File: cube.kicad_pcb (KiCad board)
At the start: 2 copper layers, 300 parts, among them J1 serial_conn, J10 Conn_01x01, J11 Conn_01x01, J2 shifters_common_conn, J3 Conn_01x01, J4 Conn_01x01, J5 Conn_01x01, J6 Conn_01x01, J7 Conn_01x01, J8 Conn_01x01, J9 Conn_01x01, Q1 IRF9540N, Q2 IRF9540N, Q3 IRF9540N, Q4 IRF9540N, Q5 IRF9540N, Q6 IRF9540N, Q7 IRF9540N, Q8 IRF9540N, U1 SN74HC595N_0_b, U10 SN74HC595N_3_b, U11 SN74HC595N_3_g, U12 SN74HC595N_3_r, U13 SN74HC595N_4_b, U14 SN74HC595N_4_g, U15 SN74HC595N_4_r, U16 SN74HC595N_5_b, U17 SN74HC595N_5_g, U18 SN74HC595N_5_r, U19 SN74HC595N_6_b, U2 SN74HC595N_0_g, U20 SN74HC595N_6_g, U21 SN74HC595N_6_r, U22 SN74HC595N_7_b, U23 SN74HC595N_7_g, U24 SN74HC595N_7_r, U25 SN74HC595N_cols, U3 SN74HC595N_0_r, U4 SN74HC595N_1_b, U5 SN74HC595N_1_g, U6 SN74HC595N_1_r, U7 SN74HC595N_2_b, U8 SN74HC595N_2_g, U9 SN74HC595N_2_r

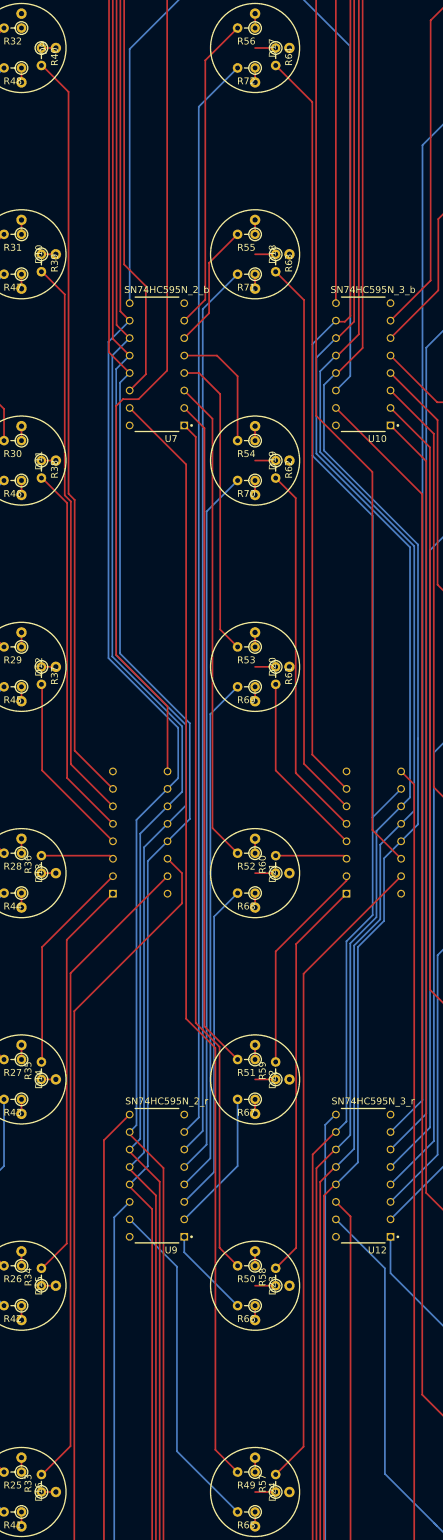
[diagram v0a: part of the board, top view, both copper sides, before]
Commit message: fix 3rd rows's green conns
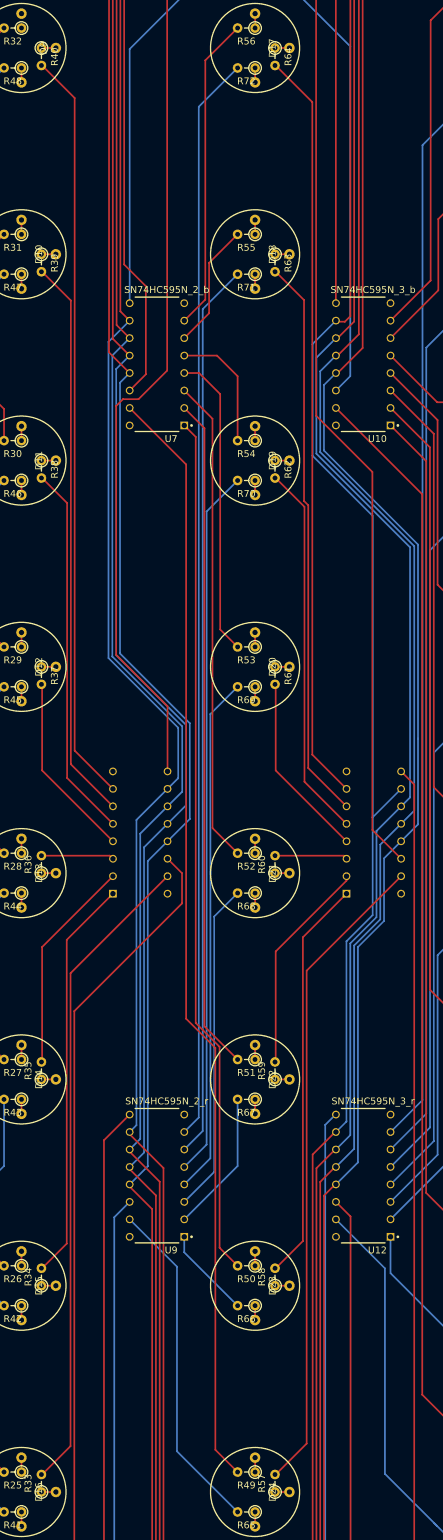
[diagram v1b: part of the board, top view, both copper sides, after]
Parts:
- moved R57 0.10 mm to (106.9, 300.0)
- moved R58 0.10 mm to (106.9, 270.0)
- moved R59 0.10 mm to (106.9, 240.0)
- moved R60 0.10 mm to (106.9, 210.0)
- moved R61 0.10 mm to (106.9, 180.0)
- moved R62 0.10 mm to (106.9, 150.0)
- moved R63 0.10 mm to (106.9, 120.0)
- moved R64 0.10 mm to (106.9, 90.0)
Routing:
- net led_2_7_g: track 3.00 -> 2.10 mm
- net led_2_6_g: track 3.00 -> 2.10 mm
- net led_2_5_g: track 3.00 -> 2.10 mm
- net led_2_4_g: track 3.00 -> 2.10 mm
- net led_2_3_g: track 3.00 -> 2.10 mm
- net led_2_2_g: track 3.00 -> 2.10 mm
- net led_2_1_g: track 3.00 -> 2.10 mm
- net led_2_0_g: track 3.00 -> 2.10 mm

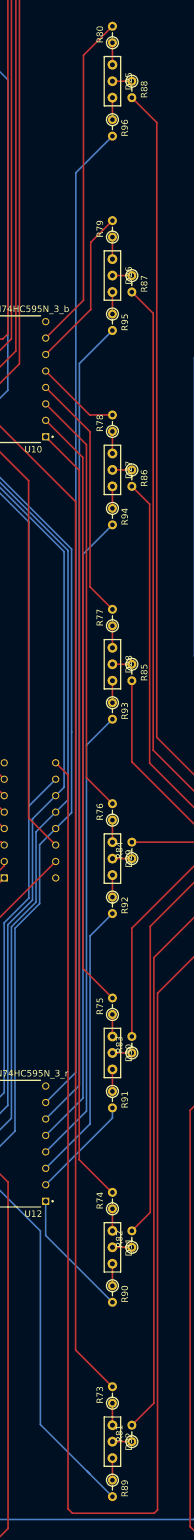
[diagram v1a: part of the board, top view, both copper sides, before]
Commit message: fix 4th rows's red conns
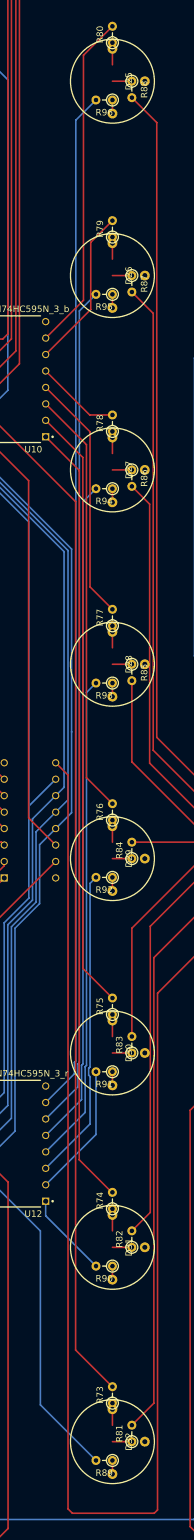
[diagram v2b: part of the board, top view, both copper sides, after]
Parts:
- moved R89 3.04 mm to (134.0, 302.9), turned to 180 degrees
- moved R90 3.04 mm to (134.0, 272.9), turned to 180 degrees
- moved R91 3.04 mm to (134.0, 242.9), turned to 180 degrees
- moved R92 3.04 mm to (134.0, 212.9), turned to 180 degrees
- moved R93 3.04 mm to (134.0, 182.9), turned to 180 degrees
- moved R94 3.04 mm to (134.0, 152.9), turned to 180 degrees
- moved R95 3.04 mm to (134.0, 122.9), turned to 180 degrees
- moved R96 3.04 mm to (134.0, 92.9), turned to 180 degrees
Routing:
- net Net-(R89-Pad2): track 56.3 -> 49.1 mm
- net Net-(R90-Pad2): track 19.9 -> 13.2 mm
- net Net-(R92-Pad2): track 43.6 -> 48.3 mm
- net Net-(R91-Pad2): track 16.1 -> 20.7 mm
- net Net-(R95-Pad2): track 126.0 -> 130.5 mm
- net Net-(R96-Pad2): track 153.4 -> 158.0 mm
- net Net-(R94-Pad2): track 98.5 -> 103.0 mm
- net Net-(R93-Pad2): track 71.1 -> 75.6 mm
- net led_3_5_r: track 3.40 -> 2.10 mm
- net led_3_4_r: track 3.40 -> 2.10 mm
- net led_3_3_r: track 3.40 -> 2.10 mm
- net led_3_2_r: track 3.40 -> 2.10 mm
- net led_3_1_r: track 3.40 -> 2.10 mm
- net led_3_0_r: track 3.40 -> 2.10 mm
- net led_3_7_r: track 3.40 -> 2.10 mm
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
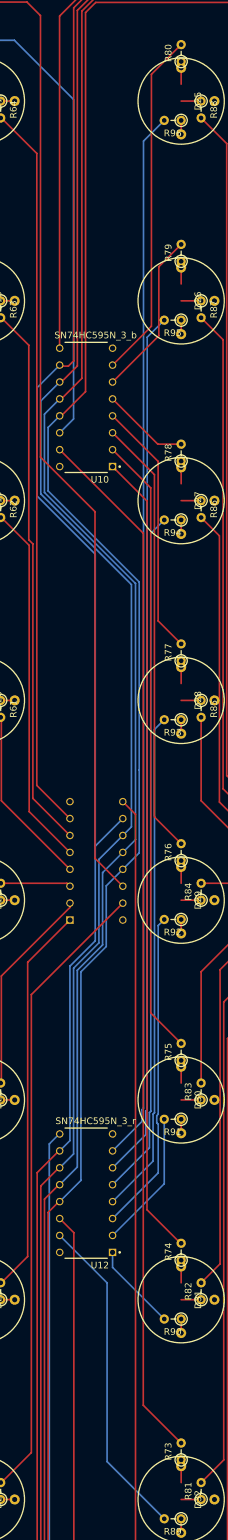
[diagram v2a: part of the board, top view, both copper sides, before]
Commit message: fix 4th rows's blue conns
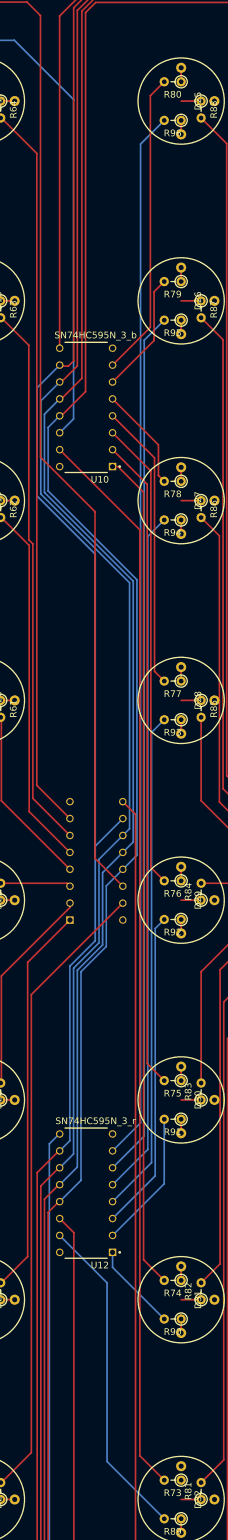
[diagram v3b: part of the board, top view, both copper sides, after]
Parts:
- moved R73 3.04 mm to (134.0, 297.1), turned to 180 degrees
- moved R74 3.04 mm to (134.0, 267.1), turned to 180 degrees
- moved R75 3.04 mm to (134.0, 237.1), turned to 180 degrees
- moved R76 3.04 mm to (134.0, 207.1), turned to 180 degrees
- moved R77 3.04 mm to (134.0, 177.1), turned to 180 degrees
- moved R78 3.04 mm to (134.0, 147.1), turned to 180 degrees
- moved R79 3.04 mm to (134.0, 117.1), turned to 180 degrees
- moved R80 3.04 mm to (134.0, 87.1), turned to 180 degrees
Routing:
- net Net-(R80-Pad2): track 52.4 -> 45.8 mm
- net Net-(R79-Pad2): track 24.9 -> 18.3 mm
- net Net-(R74-Pad2): track 121.0 -> 125.9 mm
- net Net-(R75-Pad2): track 93.4 -> 98.0 mm
- net Net-(R76-Pad2): track 66.0 -> 70.5 mm
- net Net-(R77-Pad2): track 38.5 -> 43.0 mm
- net Net-(R73-Pad2): track 156.7 -> 161.3 mm
- net led_3_7_b: track 3.40 -> 0.00 mm
- net Net-(R78-Pad2): track 13.1 -> 15.6 mm
- net led_3_5_b: track 3.40 -> 2.10 mm
- net led_3_4_b: track 3.40 -> 2.10 mm
- net led_3_3_b: track 3.40 -> 2.10 mm
- net led_3_2_b: track 3.40 -> 2.10 mm
- net led_3_1_b: track 3.40 -> 2.10 mm
- net led_3_0_b: track 3.40 -> 2.10 mm
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
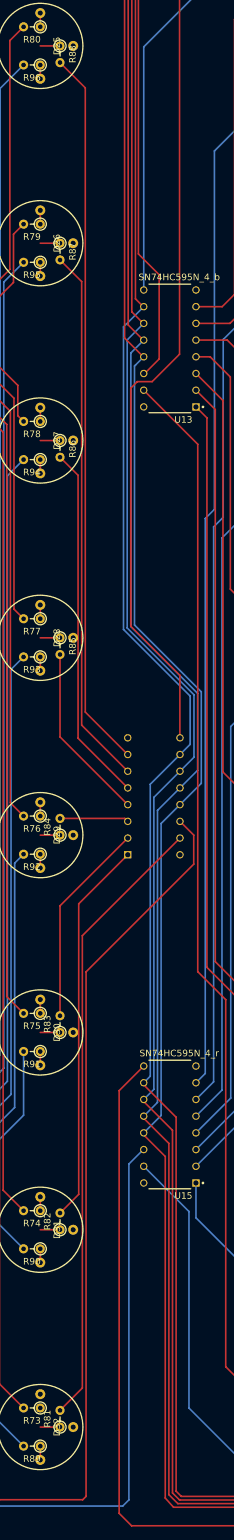
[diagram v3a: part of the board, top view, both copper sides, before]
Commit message: fix 4th rows's green conns
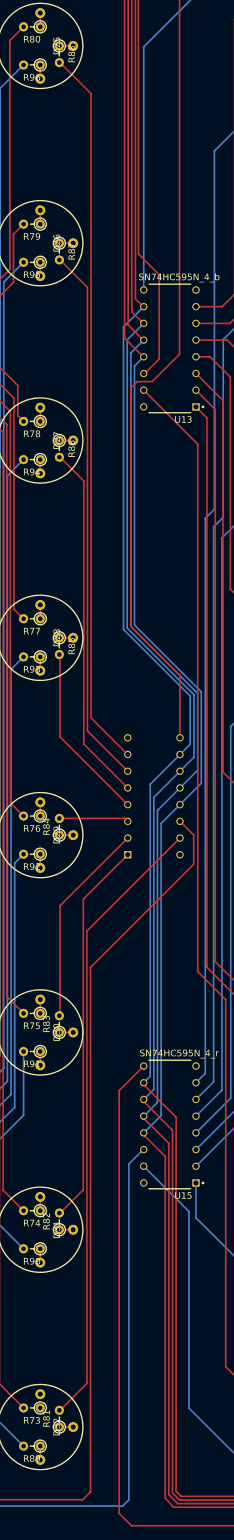
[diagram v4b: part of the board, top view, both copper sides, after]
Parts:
- moved R81 0.10 mm to (136.9, 300.0)
- moved R82 0.10 mm to (136.9, 270.0)
- moved R83 0.10 mm to (136.9, 240.0)
- moved R84 0.10 mm to (136.9, 210.0)
- moved R85 0.10 mm to (136.9, 180.0)
- moved R86 0.10 mm to (136.9, 150.0)
- moved R87 0.10 mm to (136.9, 120.0)
- moved R88 0.10 mm to (136.9, 90.0)
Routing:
- net led_3_7_g: track 3.00 -> 2.10 mm
- net led_3_6_g: track 3.00 -> 2.10 mm
- net led_3_5_g: track 3.00 -> 2.10 mm
- net led_3_4_g: track 3.00 -> 2.10 mm
- net led_3_3_g: track 3.00 -> 2.10 mm
- net led_3_2_g: track 3.00 -> 2.10 mm
- net led_3_1_g: track 3.00 -> 2.10 mm
- net led_3_0_g: track 3.00 -> 2.10 mm

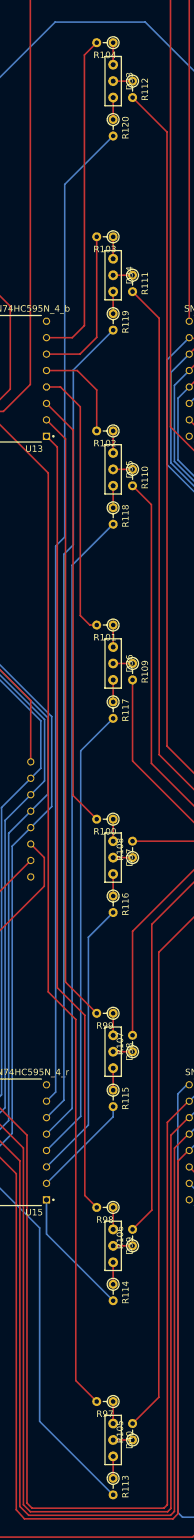
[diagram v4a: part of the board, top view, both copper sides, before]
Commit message: fix 5th rows's red conns
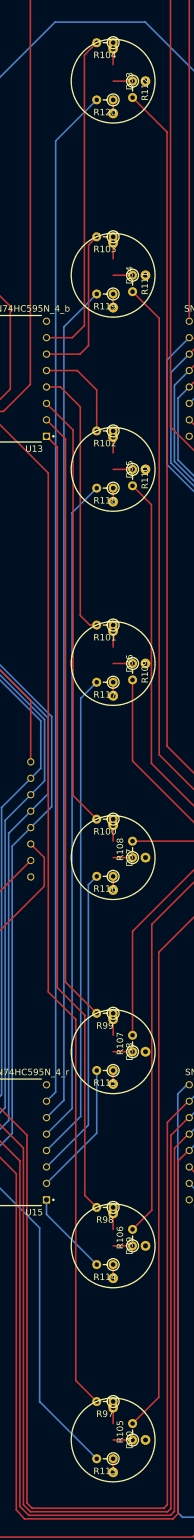
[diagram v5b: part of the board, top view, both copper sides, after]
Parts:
- moved R113 3.04 mm to (167.9, 302.9), turned to 180 degrees
- moved R114 3.04 mm to (167.9, 272.9), turned to 180 degrees
- moved R115 3.04 mm to (167.9, 242.9), turned to 180 degrees
- moved R116 3.04 mm to (167.9, 212.9), turned to 180 degrees
- moved R117 3.04 mm to (167.9, 182.9), turned to 180 degrees
- moved R118 3.04 mm to (167.9, 152.9), turned to 180 degrees
- moved R119 3.04 mm to (167.9, 122.9), turned to 180 degrees
- moved R120 3.04 mm to (167.9, 92.9), turned to 180 degrees
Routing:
- net Net-(R114-Pad2): track 19.9 -> 13.2 mm
- net Net-(R113-Pad2): track 55.7 -> 49.1 mm
- net Net-(R116-Pad2): track 43.6 -> 48.1 mm
- net Net-(R115-Pad2): track 16.1 -> 20.7 mm
- net Net-(R120-Pad2): track 153.4 -> 158.0 mm
- net Net-(R117-Pad2): track 71.1 -> 75.6 mm
- net Net-(R118-Pad2): track 98.5 -> 103.0 mm
- net Net-(R119-Pad2): track 126.0 -> 130.5 mm
- net led_4_5_r: track 3.40 -> 2.10 mm
- net led_4_4_r: track 3.40 -> 2.10 mm
- net led_4_3_r: track 3.40 -> 2.10 mm
- net led_4_2_r: track 3.40 -> 2.10 mm
- net led_4_1_r: track 3.40 -> 2.10 mm
- net led_4_0_r: track 3.40 -> 2.10 mm
- net led_4_7_r: track 3.40 -> 2.10 mm
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
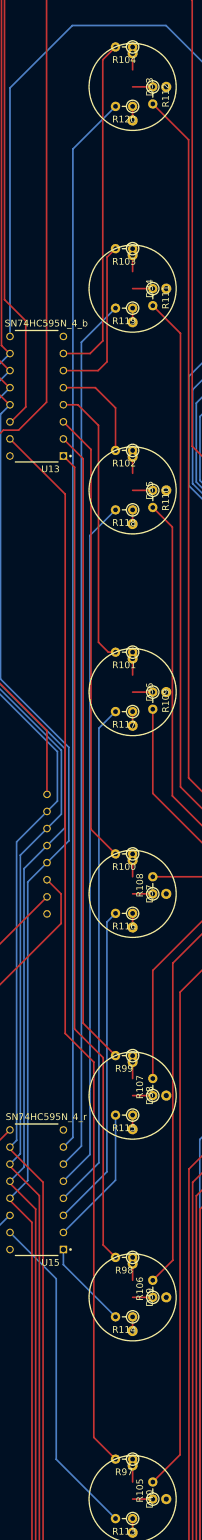
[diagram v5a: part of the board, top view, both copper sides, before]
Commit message: fix 5th rows's blue conns
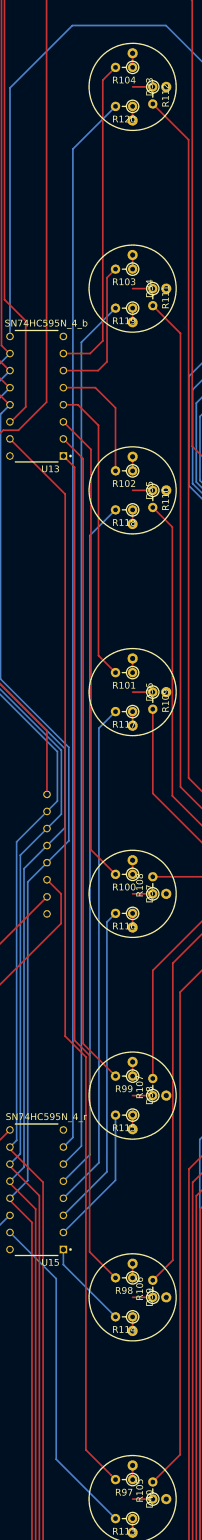
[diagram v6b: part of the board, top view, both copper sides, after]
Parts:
- moved R100 3.04 mm to (167.9, 207.1)
- moved R97 3.04 mm to (167.9, 297.1)
- moved R98 3.04 mm to (167.9, 267.1)
- moved R101 3.04 mm to (167.9, 177.1)
- moved R102 3.04 mm to (167.9, 147.1)
- moved R103 3.04 mm to (167.9, 117.1)
- moved R104 3.04 mm to (167.9, 87.1)
- moved R99 3.04 mm to (167.9, 237.1)
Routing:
- net Net-(R97-Pad2): track 158.3 -> 161.4 mm
- net Net-(R99-Pad2): track 94.9 -> 98.0 mm
- net Net-(R100-Pad2): track 67.5 -> 70.5 mm
- net Net-(R98-Pad2): track 122.4 -> 125.4 mm
- net Net-(R103-Pad2): track 24.4 -> 21.3 mm
- net Net-(R104-Pad2): track 51.1 -> 48.1 mm
- net Net-(R102-Pad2): track 15.3 -> 18.4 mm
- net Net-(R101-Pad2): track 41.9 -> 44.3 mm
- net led_4_5_b: track 3.40 -> 2.10 mm
- net led_4_4_b: track 3.40 -> 2.10 mm
- net led_4_3_b: track 3.40 -> 2.10 mm
- net led_4_2_b: track 3.40 -> 2.10 mm
- net led_4_1_b: track 3.40 -> 2.10 mm
- net led_4_0_b: track 3.40 -> 2.10 mm
- net led_4_7_b: track 3.40 -> 2.10 mm
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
